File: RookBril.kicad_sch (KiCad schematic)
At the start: 34 parts, among them J2 IR_SENSOR0_PINS, J3 IR_SENSOR1_PINS, J4 IR_SENSOR2_PINS, J5 IR_SENSOR3_PINS, J6 LOW-BAT_LED_CONN, J7 PDLC_JST_PINS, Q2 NMOS, U1 VNH7070ASTR

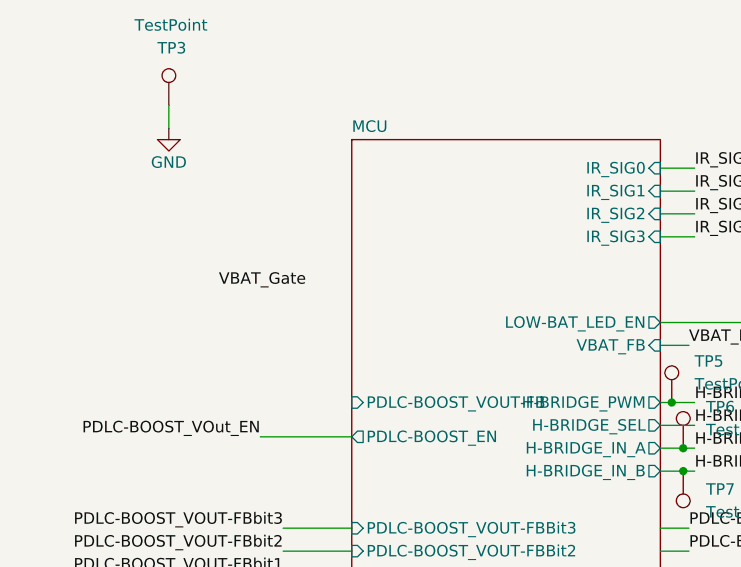
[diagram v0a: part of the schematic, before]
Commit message: PCB4Lv0.2
Paar dingen nog extra vergeten, IR LED toegevoegd aan de bottom side.
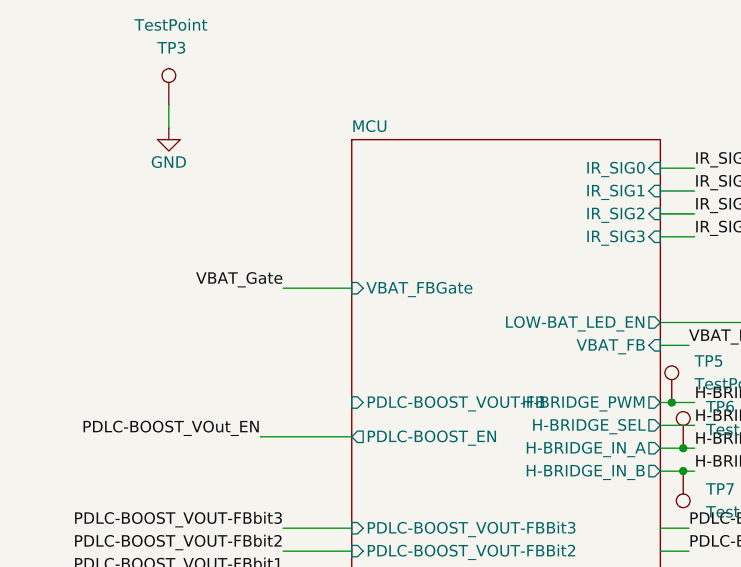
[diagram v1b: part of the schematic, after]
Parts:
- C1: footprint Capacitor_SMD:C_0805_2012Metric_Pad1.18x1.45mm_HandSolder -> Components:IRLED
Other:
- sheet MCU ports: added VBAT_FBGate; removed none
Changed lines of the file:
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@@
+    (stroke (width 0) (type default))
+  )
+  (wire (pts (xy 40.64 95.25) (xy 48.26 95.25))
     (stroke (width 0) (type default))
   )
@@
     (effects (font (size 1.27 1.27)) (justify left bottom))
   )
-  (label "VBAT_Gate" (at 43.18 95.25 180) (fields_autoplaced)
+  (label "VBAT_Gate" (at 40.64 95.25 180) (fields_autoplaced)
     (effects (font (size 1.27 1.27)) (justify right bottom))
   )
@@
       (effects (font (size 1.27 1.27)) (justify left))
     )
-    (property "Footprint" "Capacitor_SMD:C_0805_2012Metric_Pad1.18x1.45mm_HandSolder" (at 209.2452 38.735 0)
+    (property "Footprint" "Components:IRLED" (at 209.2452 38.735 0)
       (effects (font (size 1.27 1.27)) hide)
     )
@@
       (effects (font (size 1.27 1.27)) (justify left))
     )
+    (pin "VBAT_FBGate" input (at 48.26 95.25 180)
+      (effects (font (size 1.27 1.27)) (justify left))
+    )

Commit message: Ordered this one
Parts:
- C1: footprint Components:IRLED -> Capacitor_SMD:C_0805_2012Metric_Pad1.18x1.45mm_HandSolder
- renumbered TP6 to INA1, TP7 to INB1, TP5 to PWM1
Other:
- sheet MCU ports: added none; removed PDLC-BOOST_VOUT-FB
- moved on the sheet: INA1, INB1
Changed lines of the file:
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@@
 (kicad_sch (version 20230121) (generator eeschema)
   (paper "A4")
+  (junction (at 85.09 115.57) (diameter 0) (color 0 0 0 0)
+  )
   (junction (at 208.28 28.575) (diameter 0) (color 0 0 0 0)
   )
@@
   (junction (at 252.73 59.69) (diameter 0) (color 0 0 0 0)
   )
-  (junction (at 85.09 115.57) (diameter 0) (color 0 0 0 0)
+  (junction (at 85.09 119.38) (diameter 0) (color 0 0 0 0)
   )
   (junction (at 151.13 64.77) (diameter 0) (color 0 0 0 0)
-  )
-  (junction (at 85.09 113.03) (diameter 0) (color 0 0 0 0)
   )
   (junction (at 189.23 102.235) (diameter 0) (color 0 0 0 0)
@@
     (stroke (width 0) (type default))
   )
-  (wire (pts (xy 82.55 121.92) (xy 85.725 121.92))
-    (stroke (width 0) (type default))
-  )
   (wire (pts (xy 204.47 28.575) (xy 208.28 28.575))
     (stroke (width 0) (type default))
@@
     (stroke (width 0) (type default))
   )
-  (wire (pts (xy 82.55 113.03) (xy 85.09 113.03))
+  (wire (pts (xy 82.55 115.57) (xy 85.09 115.57))
     (stroke (width 0) (type default))
   )
@@
     (stroke (width 0) (type default))
   )
+  (wire (pts (xy 85.09 115.57) (xy 86.36 115.57))
+    (stroke (width 0) (type default))
+  )
   (wire (pts (xy 33.02 44.45) (xy 33.02 46.99))
     (stroke (width 0) (type default))
@@
     (stroke (width 0) (type default))
   )
-  (wire (pts (xy 85.09 115.57) (xy 86.36 115.57))
-    (stroke (width 0) (type default))
-  )
-  (wire (pts (xy 82.55 115.57) (xy 85.09 115.57))
+  (wire (pts (xy 85.09 119.38) (xy 86.36 119.38))
+    (stroke (width 0) (type default))
+  )
+  (wire (pts (xy 82.55 119.38) (xy 85.09 119.38))
     (stroke (width 0) (type default))
   )
@@
     (stroke (width 0) (type default))
   )
-  (wire (pts (xy 82.55 124.46) (xy 85.725 124.46))
-    (stroke (width 0) (type default))
-  )
   (wire (pts (xy 195.58 64.77) (xy 195.58 68.58))
     (stroke (width 0) (type default))
@@
   )
   (wire (pts (xy 198.755 71.12) (xy 198.755 62.23))
-    (stroke (width 0) (type default))
-  )
-  (wire (pts (xy 85.09 113.03) (xy 86.36 113.03))
     (stroke (width 0) (type default))
   )
@@
     (effects (font (size 1.27 1.27)) (justify left bottom))
   )
-  (label "H-BRIDGE_IN_B" (at 86.36 115.57 0) (fields_autoplaced)
+  (label "H-BRIDGE_IN_B" (at 86.36 119.38 0) (fields_autoplaced)
     (effects (font (size 1.27 1.27)) (justify left bottom))
   )
@@
     (effects (font (size 1.27 1.27)) (justify right bottom))
   )
-  (label "PDLC-BOOST_VOUT-FB" (at 85.725 124.46 0) (fields_autoplaced)
-    (effects (font (size 1.27 1.27)) (justify left bottom))
-  )
   (label "VBAT_FB" (at 85.725 101.6 0) (fields_autoplaced)
     (effects (font (size 1.27 1.27)) (justify left bottom))
@@
     (effects (font (size 1.27 1.27)) (justify right bottom))
   )
-  (label "PDLC-BOOST_CTRL" (at 85.725 121.92 0) (fields_autoplaced)
-    (effects (font (size 1.27 1.27)) (justify left bottom))
-  )
   (label "IR_SIG3" (at 244.475 71.12 0) (fields_autoplaced)
     (effects (font (size 1.27 1.27)) (justify left bottom))
@@
     (effects (font (size 1.27 1.27)) (justify left bottom))
   )
-  (label "H-BRIDGE_IN_A" (at 86.36 113.03 0) (fields_autoplaced)
+  (label "H-BRIDGE_IN_A" (at 86.36 115.57 0) (fields_autoplaced)
     (effects (font (size 1.27 1.27)) (justify left bottom))
   )
@@
     )
   )
-  (symbol (lib_id "Connector:TestPoint") (at 85.09 115.57 180) (unit 1)
-    (in_bom yes) (on_board yes) (dnp no) (fields_autoplaced)
-    (property "Reference" "TP7" (at 87.63 117.602 0)
+  (symbol (lib_id "Connector:TestPoint") (at 85.09 119.38 180) (unit 1)
+    (in_bom yes) (on_board yes) (dnp no)
+    (property "Reference" "INB1" (at 87.63 121.412 0)
       (effects (font (size 1.27 1.27)) (justify right))
     )
-    (property "Value" "TestPoint" (at 87.63 120.142 0)
+    (property "Value" "TestPoint" (at 92.71 121.92 0)
       (effects (font (size 1.27 1.27)) (justify right))
     )
-    (property "Footprint" "TestPoint:TestPoint_Pad_D1.0mm" (at 80.01 115.57 0)
-      (effects (font (size 1.27 1.27)) hide)
-    )
-    (property "Datasheet" "~" (at 80.01 115.57 0)
-      (effects (font (size 1.27 1.27)) hide)
-    )
-    (pin "1")
-    (instances
-      (project "RookBril"
-        (path "/5dc439a9-720d-4bdc-b61f-78a76fde4df5"
-          (reference "TP7") (unit 1)
+    (property "Footprint" "TestPoint:TestPoint_Pad_D1.0mm" (at 80.01 119.38 0)
+      (effects (font (size 1.27 1.27)) hide)
+    )
+    (property "Datasheet" "~" (at 80.01 119.38 0)
+      (effects (font (size 1.27 1.27)) hide)
+    )
+    (pin "1")
+    (instances
+      (project "RookBril"
+        (path "/5dc439a9-720d-4bdc-b61f-78a76fde4df5"
+          (reference "INB1") (unit 1)
         )
       )
@@
     )
   )
-  (symbol (lib_id "Connector:TestPoint") (at 85.09 113.03 0) (unit 1)
-    (in_bom yes) (on_board yes) (dnp no) (fields_autoplaced)
-    (property "Reference" "TP6" (at 87.63 108.458 0)
-      (effects (font (size 1.27 1.27)) (justify left))
-    )
-    (property "Value" "TestPoint" (at 87.63 110.998 0)
-      (effects (font (size 1.27 1.27)) (justify left))
-    )
-    (property "Footprint" "TestPoint:TestPoint_Pad_D1.0mm" (at 90.17 113.03 0)
-      (effects (font (size 1.27 1.27)) hide)
-    )
-    (property "Datasheet" "~" (at 90.17 113.03 0)
-      (effects (font (size 1.27 1.27)) hide)
-    )
-    (pin "1")
-    (instances
-      (project "RookBril"
-        (path "/5dc439a9-720d-4bdc-b61f-78a76fde4df5"
-          (reference "TP6") (unit 1)
+  (symbol (lib_id "Connector:TestPoint") (at 85.09 115.57 0) (unit 1)
+    (in_bom yes) (on_board yes) (dnp no)
+    (property "Reference" "INA1" (at 87.63 111.76 0)
+      (effects (font (size 1.27 1.27)) (justify left))
+    )
+    (property "Value" "TestPoint" (at 92.71 111.76 0)
+      (effects (font (size 1.27 1.27)) (justify left))
+    )
+    (property "Footprint" "TestPoint:TestPoint_Pad_D1.0mm" (at 90.17 115.57 0)
+      (effects (font (size 1.27 1.27)) hide)
+    )
+    (property "Datasheet" "~" (at 90.17 115.57 0)
+      (effects (font (size 1.27 1.27)) hide)
+    )
+    (pin "1")
+    (instances
+      (project "RookBril"
+        (path "/5dc439a9-720d-4bdc-b61f-78a76fde4df5"
+          (reference "INA1") (unit 1)
         )
       )
@@
     )
     (pin "1")
+    (pin "2")
     (pin "3")
-    (pin "2")
     (instances
       (project "RookBril"
@@
   )
   (symbol (lib_id "Connector:TestPoint") (at 83.82 107.95 0) (unit 1)
-    (in_bom yes) (on_board yes) (dnp no) (fields_autoplaced)
-    (property "Reference" "TP5" (at 86.36 103.378 0)
-      (effects (font (size 1.27 1.27)) (justify left))
-    )
-    (property "Value" "TestPoint" (at 86.36 105.918 0)
+    (in_bom yes) (on_board yes) (dnp no)
+    (property "Reference" "PWM1" (at 86.36 104.14 0)
+      (effects (font (size 1.27 1.27)) (justify left))
+    )
+    (property "Value" "TestPoint" (at 91.44 104.14 0)
       (effects (font (size 1.27 1.27)) (justify left))
     )
@@
       (project "RookBril"
         (path "/5dc439a9-720d-4bdc-b61f-78a76fde4df5"
-          (reference "TP5") (unit 1)
+          (reference "PWM1") (unit 1)
         )
       )
@@
       (effects (font (size 1.27 1.27)) (justify left))
     )
-    (property "Footprint" "Components:IRLED" (at 209.2452 38.735 0)
+    (property "Footprint" "Capacitor_SMD:C_0805_2012Metric_Pad1.18x1.45mm_HandSolder" (at 209.2452 38.735 0)
       (effects (font (size 1.27 1.27)) hide)
     )
@@
       (effects (font (size 1.27 1.27)) (justify right))
     )
-    (pin "H-BRIDGE_IN_B" output (at 82.55 115.57 0)
+    (pin "H-BRIDGE_IN_B" output (at 82.55 119.38 0)
       (effects (font (size 1.27 1.27)) (justify right))
     )
-    (pin "H-BRIDGE_IN_A" output (at 82.55 113.03 0)
+    (pin "H-BRIDGE_IN_A" output (at 82.55 115.57 0)
       (effects (font (size 1.27 1.27)) (justify right))
     )
@@
       (effects (font (size 1.27 1.27)) (justify right))
     )
-    (pin "PDLC-BOOST_VOUT-FB" input (at 48.26 107.95 180)
-      (effects (font (size 1.27 1.27)) (justify left))
-    )
     (pin "PDLC-BOOST_EN" output (at 48.26 111.76 180)
